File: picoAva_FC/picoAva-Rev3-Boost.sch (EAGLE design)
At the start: 26 parts, among them IC2 TPS61201, J1 AVR_SPI_PRG_6PTH, U1 ATMEGA328

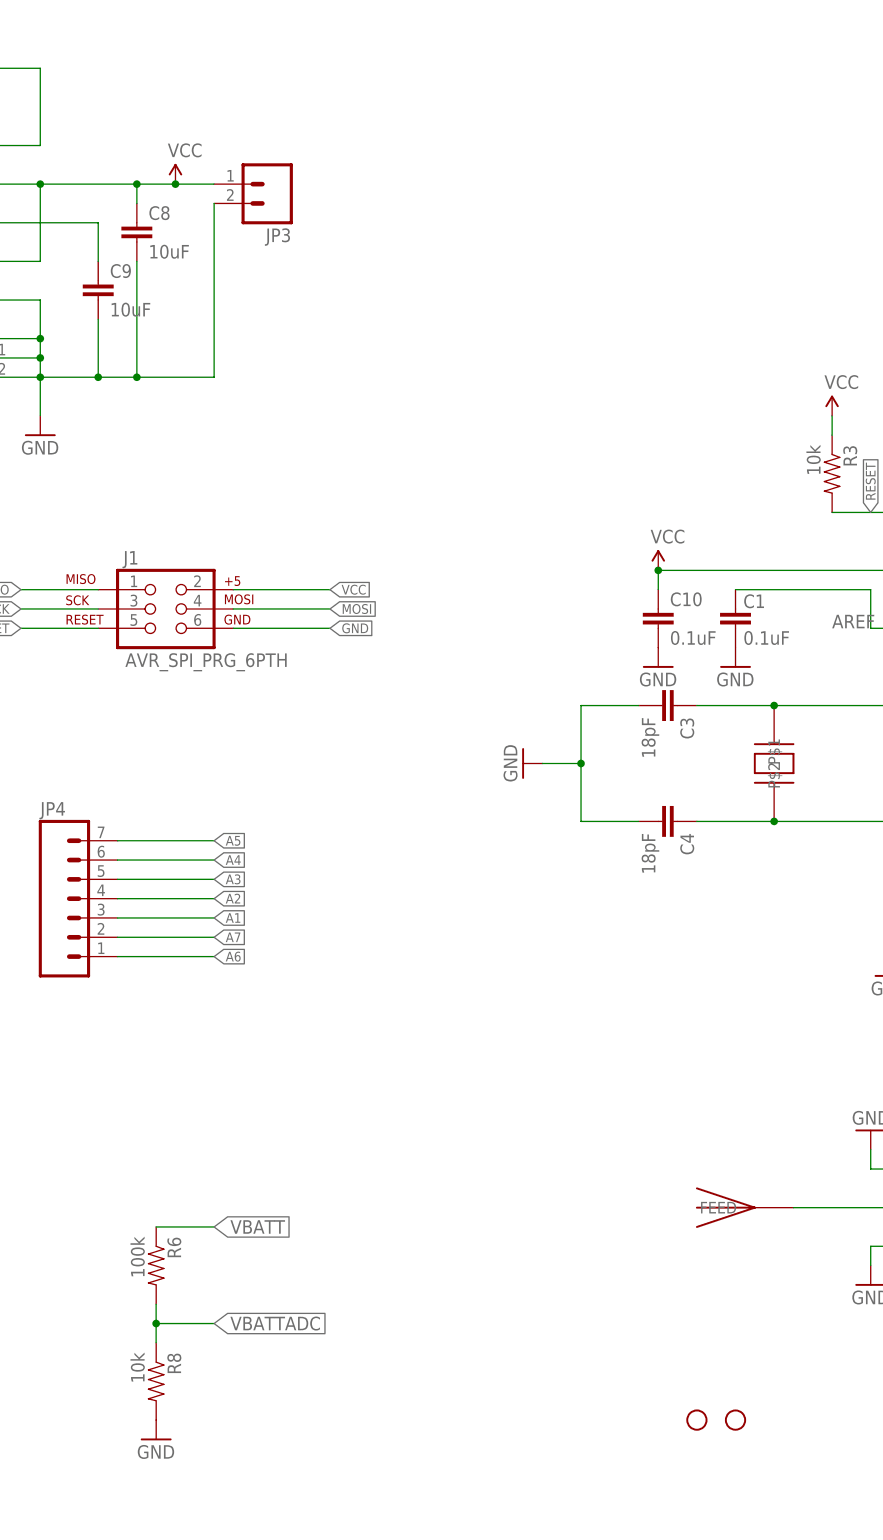
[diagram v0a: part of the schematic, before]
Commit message: Removed older versions
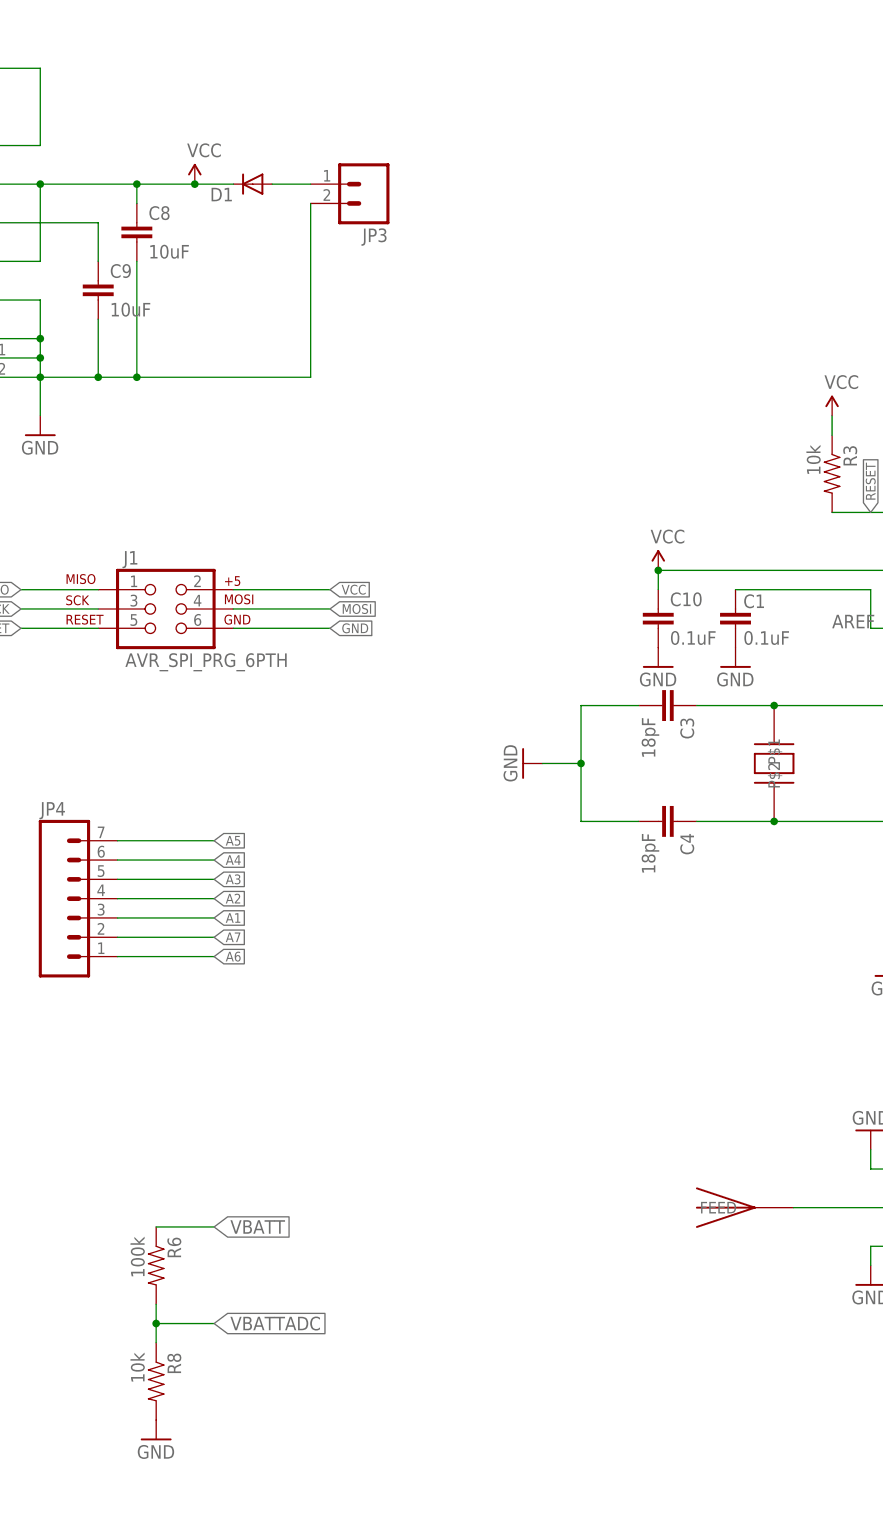
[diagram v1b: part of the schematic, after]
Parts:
- removed JP1, JP2: STAND-OFF, SparkFun:STAND-OFF
- added D1: (no value), SparkFun:DIODESMA
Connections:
- new net N$1: D1.A, JP3.1
- net VCC: now also D1.C; no longer JP3.1
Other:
- moved on the sheet: JP3
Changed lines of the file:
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@@
 <part name="C4" library="SparkFun" deviceset="CAP" device="0402-CAP" value="18pF"/>
 <part name="GND2" library="SparkFun" deviceset="GND" device=""/>
-<part name="JP1" library="SparkFun" deviceset="STAND-OFF" device=""/>
-<part name="JP2" library="SparkFun" deviceset="STAND-OFF" device=""/>
 <part name="U$2" library="ava" deviceset="ABRACON_ABM3_CRYSTAL" device=""/>
 <part name="R6" library="SparkFun" deviceset="RESISTOR" device="0402-RES" value="100k"/>
@@
 <part name="P+3" library="SparkFun" deviceset="3.3V" device="" value="VCC"/>
 <part name="U$4" library="ava" deviceset="ELLVGG_INDUCTOR" device=""/>
+<part name="D1" library="SparkFun" deviceset="DIODE" device="SMA"/>
 </parts>
 <sheets>
@@
 <instance part="C4" gate="G$1" x="172.72" y="124.46" rot="R270"/>
 <instance part="GND2" gate="1" x="154.94" y="132.08" rot="R270"/>
-<instance part="JP1" gate="G$1" x="177.8" y="45.72"/>
-<instance part="JP2" gate="G$1" x="182.88" y="45.72"/>
 <instance part="U$2" gate="G$1" x="187.96" y="132.08" rot="R90"/>
 <instance part="R6" gate="G$1" x="106.68" y="66.04" rot="R270"/>
@@
 <instance part="R3" gate="G$1" x="195.58" y="170.18" rot="R270"/>
 <instance part="P+5" gate="G$1" x="195.58" y="177.8"/>
-<instance part="JP3" gate="G$1" x="121.92" y="208.28" rot="R180"/>
+<instance part="JP3" gate="G$1" x="134.62" y="208.28" rot="R180"/>
 <instance part="JP4" gate="G$1" x="96.52" y="111.76"/>
 <instance part="IC2" gate="G$1" x="71.12" y="198.12"/>
@@
 <instance part="GND15" gate="1" x="91.44" y="175.26"/>
 <instance part="C9" gate="G$1" x="99.06" y="193.04"/>
-<instance part="P+3" gate="G$1" x="109.22" y="208.28"/>
+<instance part="P+3" gate="G$1" x="111.76" y="208.28"/>
 <instance part="U$4" gate="G$1" x="71.12" y="223.52" rot="R90"/>
+<instance part="D1" gate="G$1" x="119.38" y="208.28" rot="R180"/>
 </instances>
 <busses>
@@
 <junction x="99.06" y="182.88"/>
 <pinref part="JP3" gate="G$1" pin="2"/>
-<wire x1="114.3" y1="205.74" x2="114.3" y2="182.88" width="0.1524" layer="91"/>
-<wire x1="114.3" y1="182.88" x2="104.14" y2="182.88" width="0.1524" layer="91"/>
+<wire x1="127" y1="205.74" x2="127" y2="182.88" width="0.1524" layer="91"/>
+<wire x1="127" y1="182.88" x2="104.14" y2="182.88" width="0.1524" layer="91"/>
 <junction x="104.14" y="182.88"/>
 </segment>
@@
 <wire x1="91.44" y1="208.28" x2="104.14" y2="208.28" width="0.1524" layer="91"/>
 <pinref part="C8" gate="G$1" pin="1"/>
-<wire x1="104.14" y1="208.28" x2="109.22" y2="208.28" width="0.1524" layer="91"/>
-<wire x1="109.22" y1="208.28" x2="114.3" y2="208.28" width="0.1524" layer="91"/>
+<wire x1="104.14" y1="208.28" x2="111.76" y2="208.28" width="0.1524" layer="91"/>
 <wire x1="104.14" y1="208.28" x2="104.14" y2="205.74" width="0.1524" layer="91"/>
 <junction x="91.44" y="208.28"/>
 <junction x="104.14" y="208.28"/>
-<pinref part="JP3" gate="G$1" pin="1"/>
 <pinref part="P+3" gate="G$1" pin="3.3V"/>
-<junction x="109.22" y="208.28"/>
+<pinref part="D1" gate="G$1" pin="C"/>
+<wire x1="111.76" y1="208.28" x2="116.84" y2="208.28" width="0.1524" layer="91"/>
+<junction x="111.76" y="208.28"/>
 </segment>
 </net>
@@
 </segment>
 </net>
+<net name="N$1" class="0">
+<segment>
+<pinref part="D1" gate="G$1" pin="A"/>
+<pinref part="JP3" gate="G$1" pin="1"/>
+<wire x1="121.92" y1="208.28" x2="127" y2="208.28" width="0.1524" layer="91"/>
+</segment>
+</net>
